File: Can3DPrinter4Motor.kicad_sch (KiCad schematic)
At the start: 35 parts

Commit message: Assigning a lot of values to components Change MOSFETS for different (correct) ones Copy Motor1 to Motor2-4 Guess max current per voltage on PowerSupply schema
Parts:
- added F101, F102: 65V 20A, symbol Device:Fuse
- added J132: Heating Enable, Connector_JST:JST_XH_B2B-XH-A_1x02_P2.50mm_Vertical, symbol Connector_Generic:Conn_01x02
- D? (x5): footprint (none) -> LED_SMD:LED_0402_1005Metric; LCSC (none) -> C434448; Mouser (none) -> 720-LWQH8G-Q2S2-3K5L
- J101, J102: renamed from J?; LCSC (none) -> C234188; Mouser (none) -> 538-43045-0612
- J111, J141, J142, J143, J144: renamed from J?; LCSC (none) -> C144394
- J121, J122, J123, J124, J131: renamed from J?; LCSC (none) -> C265283
- R?: value ??? -> 600
- R?: value ??? -> 42k
- R?: value ??? -> 90k
- R?: value ??? -> 18k
- R?: value ??? -> 4k
- gave numbers to parts that had none: 13
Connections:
- net +24V: now also F101.2; no longer J101.2 (Pin_2), J102.2 (Pin_2)
- net +48V: now also F102.2; no longer J101.3 (Pin_3), J102.3 (Pin_3)
- net GND: now also J132.1 (Pin_1)
- net Heating Enable renamed Bed Heating
- new net: F101.1, J101.2 (Pin_2), J102.2 (Pin_2)
- new net: F102.1, J101.3 (Pin_3), J102.3 (Pin_3)
- new net Head Heating: J132.2 (Pin_2)
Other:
- sheet Power Supply: file Power Supply.kicad_sch -> PowerSupply.kicad_sch
- note added: "0.5mA"
- note removed: "3.3V or 5V?"

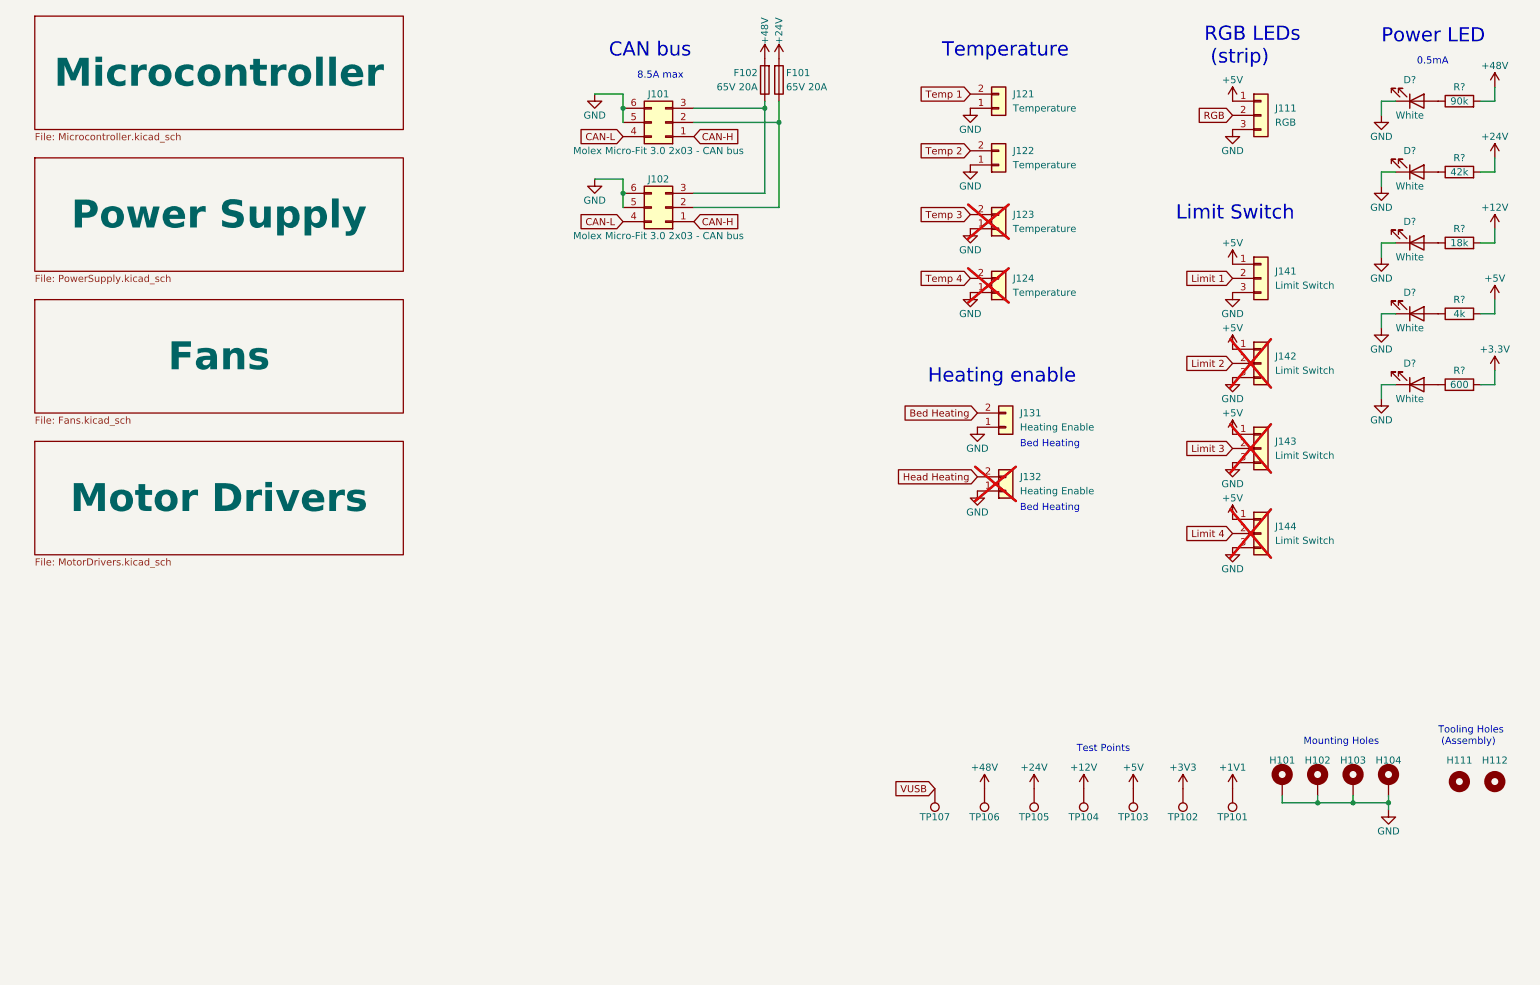
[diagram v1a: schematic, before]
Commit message: Complete schematics Assign every value (very few exceptions) Change TCM5160 from on-board to separate module Add fuses Add power supplies (LDO + 2x buck converter)
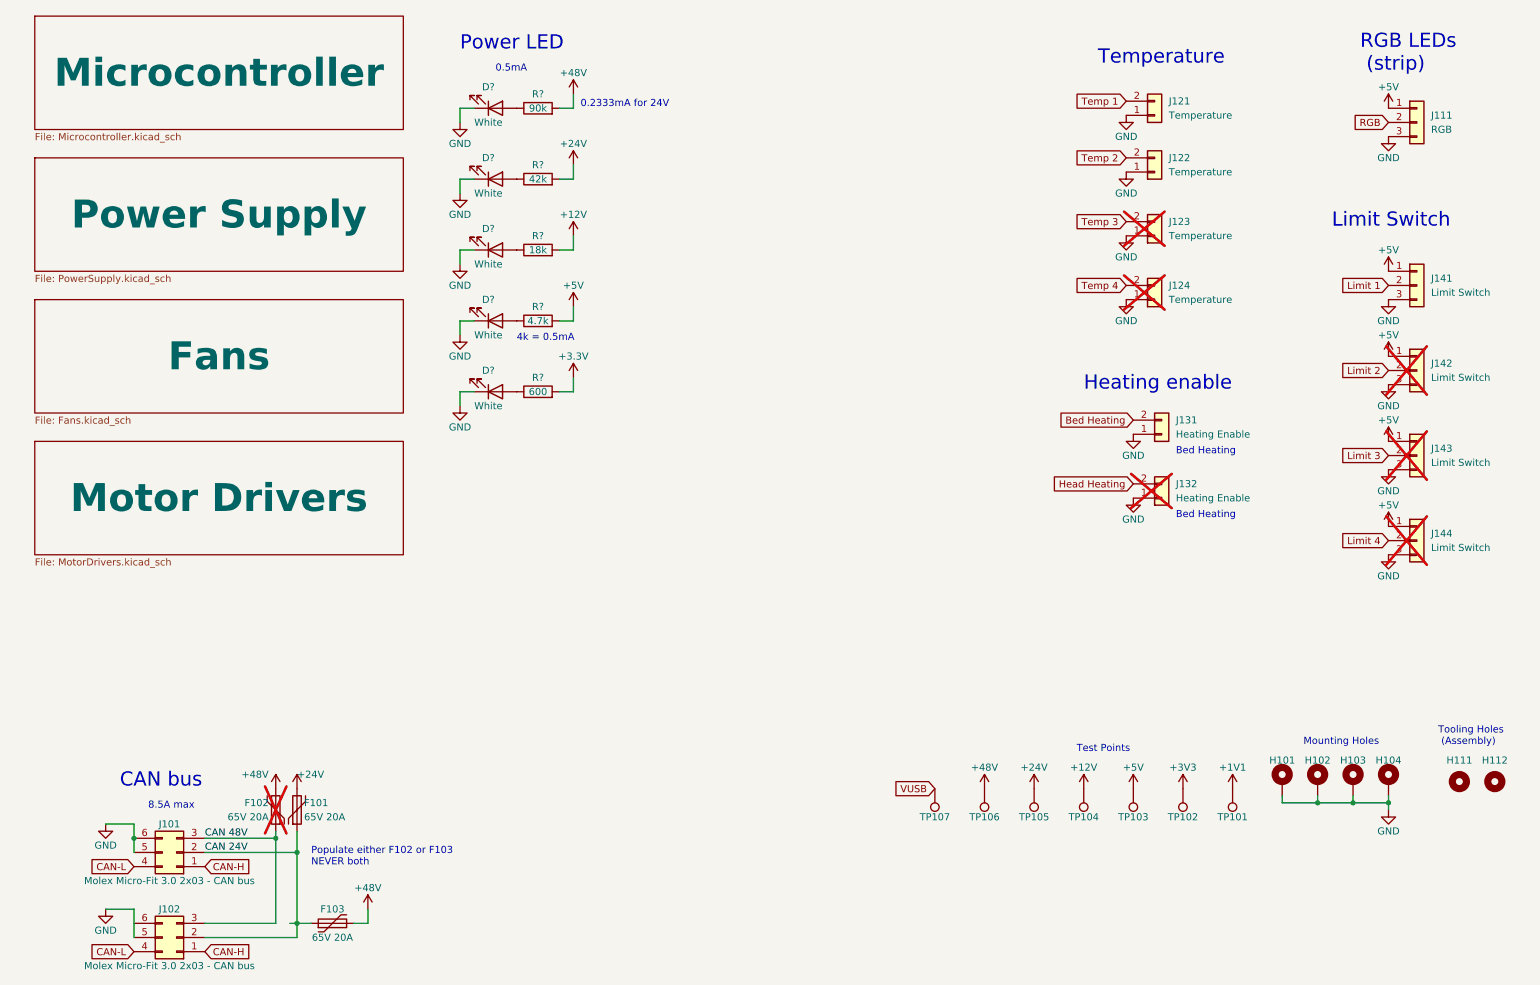
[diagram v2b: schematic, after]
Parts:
- added F103: 65V 20A, Custom:Fuse_2410_6125Metric, symbol Device:Polyfuse
- F101: footprint (none) -> Custom:Fuse_2410_6125Metric; symbol Device:Fuse -> Device:Polyfuse; LCSC (none) -> C83077
- F102: footprint (none) -> Custom:Fuse_2410_6125Metric; symbol Device:Fuse -> Device:Polyfuse; LCSC (none) -> C83077; now not fitted
- H111, H112: footprint Yautja:Tooling Hole (JLCPCB) -> Custom:Tooling Hole (JLCPCB)
- R? (x4): footprint (none) -> Resistor_SMD:R_0603_1608Metric
- R?: value 4k -> 4.7k; footprint (none) -> Resistor_SMD:R_0603_1608Metric; LCSC (none) -> C23162
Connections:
- net +48V: now also F103.2
- net GND: no longer J102.6 (Pin_6)
- net CAN 24V: now reaches F101.1, J101.2 (Pin_2), J102.2 (Pin_2)
- net CAN 24V: now also F103.1
- net CAN 48V: now reaches F102.1, J101.3 (Pin_3), J102.3 (Pin_3)
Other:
- note added: "0.2333mA for 24V"
- note added: "4k = 0.5mA"
- note added: "Populate either F102 or F103 NEVER both"
- moved on the sheet: D?, J101, J102, J111, J121, J122, J123, J124, J131, J132, J141, J142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

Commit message: WIP PCB placement, minor fixes
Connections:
- net GND: now also J102.6 (Pin_6)
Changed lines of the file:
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@@
   (junction (at 33.02 162.56) (diameter 0) (color 0 0 0 0)
+  )
+  (junction (at 33.02 177.8) (diameter 0) (color 0 0 0 0)
   )
   (junction (at 245.11 156.21) (diameter 0) (color 0 0 0 0)
@@
     (stroke (width 0) (type default))
   )
+  (wire (pts (xy 33.02 177.8) (xy 33.02 180.34))
+    (stroke (width 0) (type default))
+  )
   (wire (pts (xy 58.42 162.56) (xy 58.42 177.8))
     (stroke (width 0) (type default))
@@
     (stroke (width 0) (type default))
   )
-  (wire (pts (xy 33.02 175.26) (xy 33.02 180.34))
+  (wire (pts (xy 33.02 175.26) (xy 33.02 177.8))
     (stroke (width 0) (type default))
   )
